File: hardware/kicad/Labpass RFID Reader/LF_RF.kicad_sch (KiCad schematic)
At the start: 24 parts

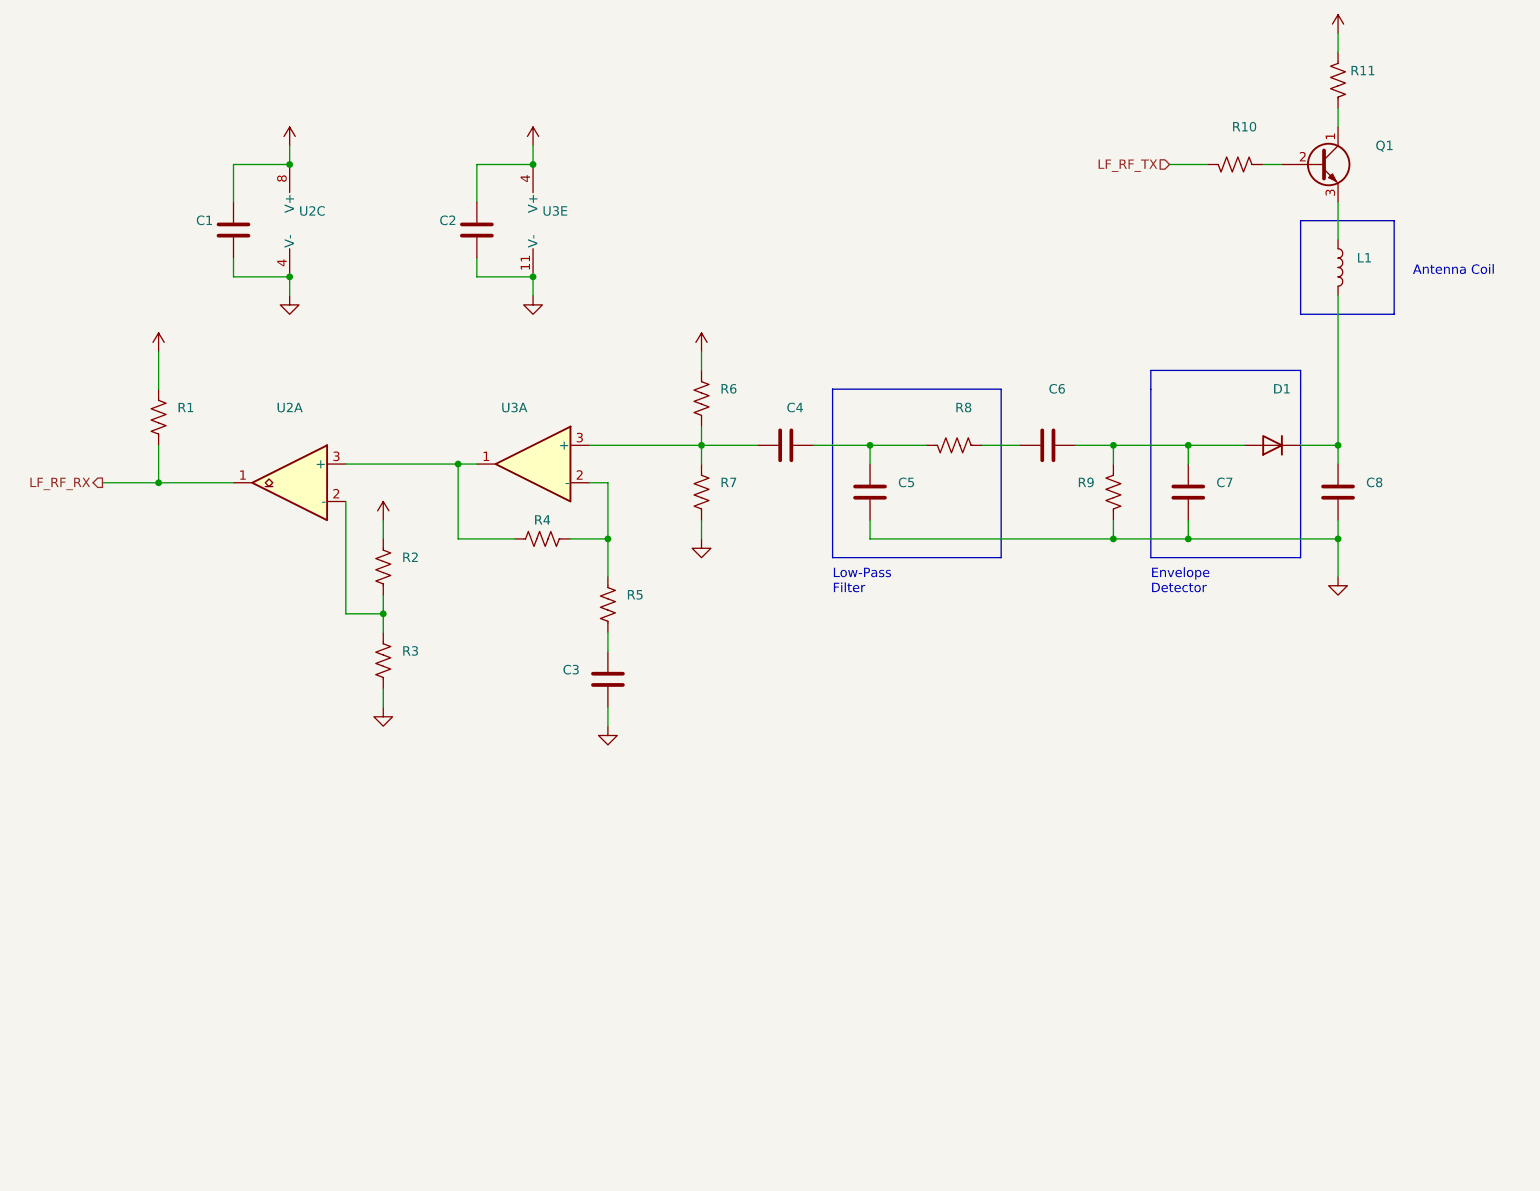
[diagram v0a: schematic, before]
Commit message: Re-do board design using kicad 6.04 stable
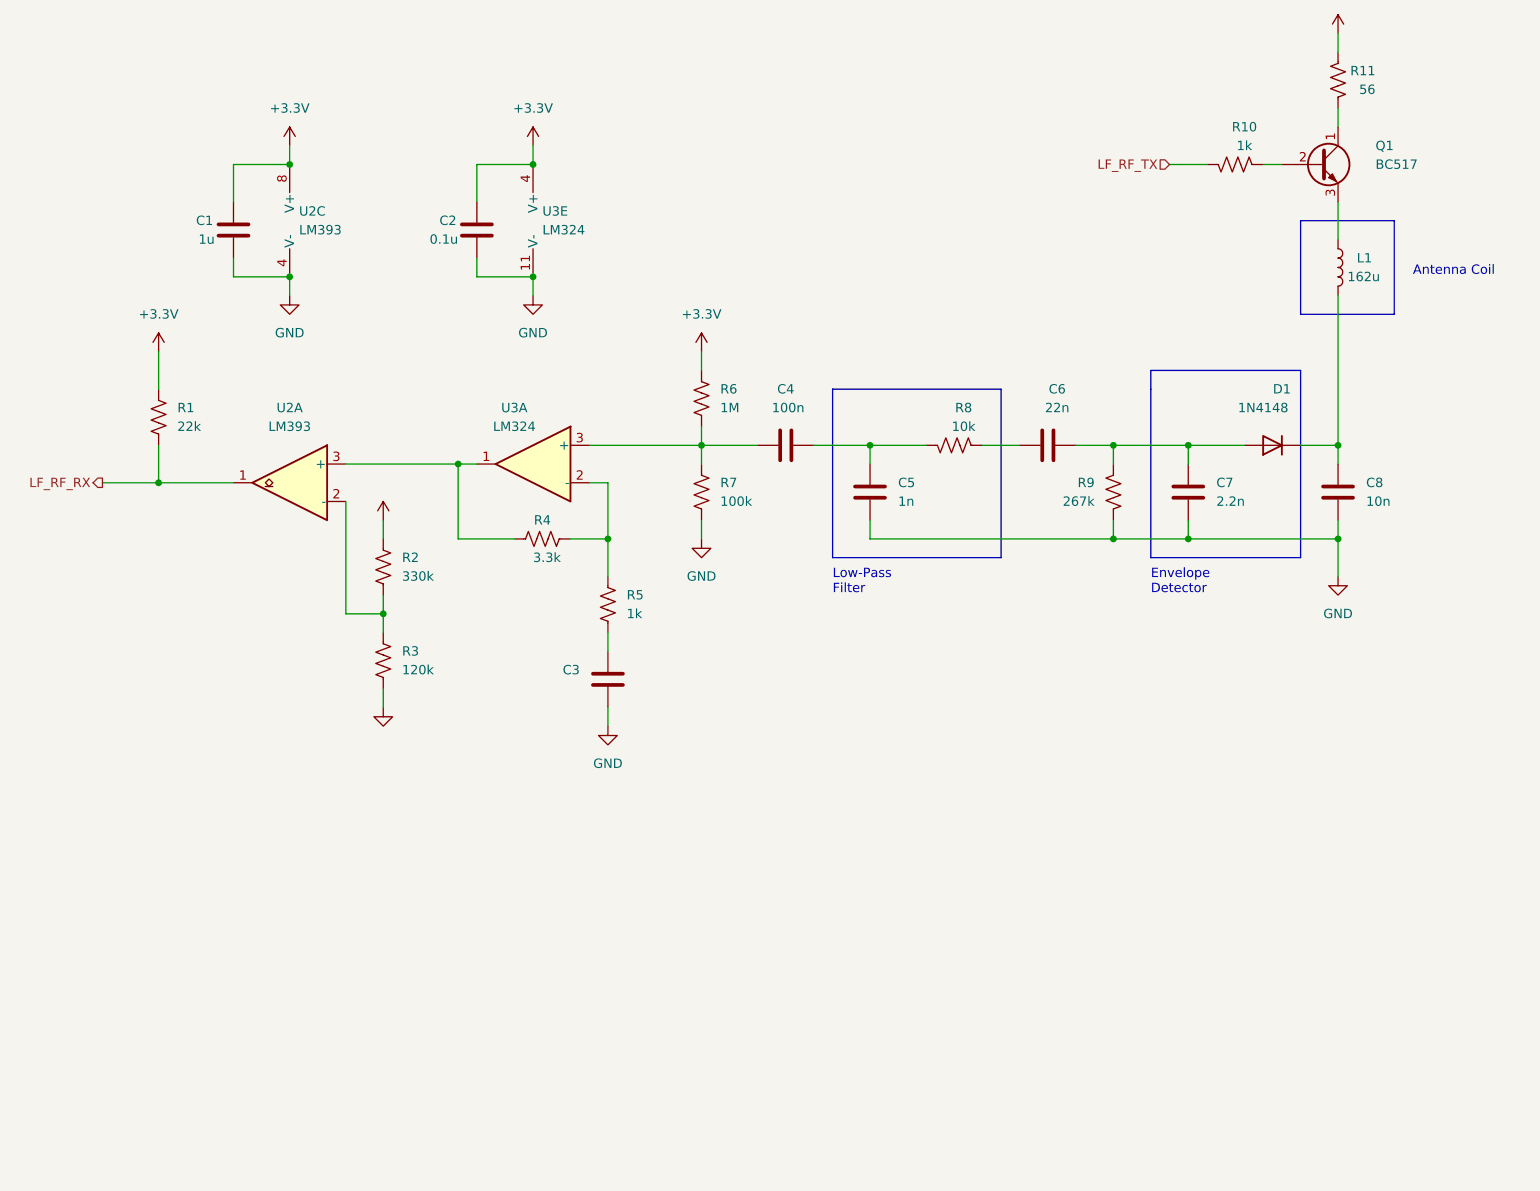
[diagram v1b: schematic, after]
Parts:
- C1: value (none) -> 1u; footprint (none) -> Capacitor_SMD:C_0603_1608Metric
- C2: value (none) -> 0.1u; footprint (none) -> Capacitor_SMD:C_0603_1608Metric
- C3: value (none) -> ~; footprint (none) -> Capacitor_SMD:C_0603_1608Metric
- C4: value (none) -> 100n; footprint (none) -> Capacitor_SMD:C_0603_1608Metric
- C5: value (none) -> 1n; footprint (none) -> Capacitor_SMD:C_0603_1608Metric
- C6: value (none) -> 22n; footprint (none) -> Capacitor_SMD:C_0603_1608Metric
- C7: value (none) -> 2.2n; footprint (none) -> Capacitor_SMD:C_0603_1608Metric
- C8: value (none) -> 10n; footprint (none) -> Capacitor_SMD:C_0603_1608Metric
- D1: value (none) -> 1N4148; footprint (none) -> Diode_SMD:D_SOD-323F
- L1: value (none) -> 162u; footprint (none) -> Connector_PinHeader_1.00mm:PinHeader_1x02_P1.00mm_Vertical_SMD_Pin1Left
- Q1: value (none) -> BC517; footprint (none) -> Package_TO_SOT_THT:TO-92
- R1: value (none) -> 22k; footprint (none) -> Resistor_SMD:R_0603_1608Metric
- R10, R5: value (none) -> 1k; footprint (none) -> Resistor_SMD:R_0603_1608Metric
- R11: value (none) -> 56; footprint (none) -> Resistor_SMD:R_0603_1608Metric
- R2: value (none) -> 330k; footprint (none) -> Resistor_SMD:R_0603_1608Metric
- R3: value (none) -> 120k; footprint (none) -> Resistor_SMD:R_0603_1608Metric
- R4: value (none) -> 3.3k; footprint (none) -> Resistor_SMD:R_0603_1608Metric
- R6: value (none) -> 1M; footprint (none) -> Resistor_SMD:R_0603_1608Metric
- R7: value (none) -> 100k; footprint (none) -> Resistor_SMD:R_0603_1608Metric
- R8: value (none) -> 10k; footprint (none) -> Resistor_SMD:R_0603_1608Metric
- R9: value (none) -> 267k; footprint (none) -> Resistor_SMD:R_0603_1608Metric
- U2: value (none) -> LM393; footprint (none) -> Package_SO:SOIC-8_3.9x4.9mm_P1.27mm
- U3: value (none) -> LM324; footprint (none) -> Package_SO:SO-14_3.9x8.65mm_P1.27mm

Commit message: kicad backups
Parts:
- removed L1: 162u, Connector_PinHeader_1.00mm:PinHeader_1x02_P1.00mm_Vertical_SMD_Pin1Left, symbol Device:L
- added J3: (no value), symbol Connector_Generic:Conn_01x02
- C1, C2: Temp Coef (none) -> X5R
- C3: value ~ -> 100n; Temp Coef (none) -> NP0
- C4, C5, C6, C7: Temp Coef (none) -> NP0
- C8: value 10n -> (none); footprint Capacitor_SMD:C_0603_1608Metric -> (none); Temp Coef (none) -> NP0
- R3: value 120k -> 110k
- R9: value 267k -> 222k
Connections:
- net at C8.1, D1.1 (K): now also J3.2 (Pin_2)
- net at Q1.3 (E): now also J3.1 (Pin_1)
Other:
- note added: "Hand-Wound rectangular coil approx 61mm X 61mm 26 AWG (.404mm dia) N = 25 L should be as close as possible to 162.1 uH"
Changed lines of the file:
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@@
     (stroke (width 0) (type default) (color 0 0 0 0))
   )
-  (polyline (pts (xy 226.06 66.04) (xy 238.76 66.04))
+  (polyline (pts (xy 227.33 66.04) (xy 240.03 66.04))
     (stroke (width 0) (type default) (color 0 0 0 0))
   )
@@
     (stroke (width 0) (type default) (color 0 0 0 0))
   )
-  (wire (pts (xy 231.14 76.2) (xy 231.14 96.52))
+  (wire (pts (xy 231.14 73.66) (xy 231.14 96.52))
     (stroke (width 0) (type default) (color 0 0 0 0))
   )
@@
     (stroke (width 0) (type default) (color 0 0 0 0))
   )
+  (polyline (pts (xy 240.03 66.04) (xy 246.38 66.04))
+    (stroke (width 0) (type default) (color 0 0 0 0))
+  )
   (wire (pts (xy 88.9 55.88) (xy 88.9 58.42))
     (stroke (width 0) (type default) (color 0 0 0 0))
@@
     (stroke (width 0) (type default) (color 0 0 0 0))
   )
-  (polyline (pts (xy 238.76 78.74) (xy 226.06 78.74))
+  (polyline (pts (xy 246.38 78.74) (xy 227.33 78.74))
     (stroke (width 0) (type default) (color 0 0 0 0))
   )
@@
     (stroke (width 0) (type default) (color 0 0 0 0))
   )
-  (wire (pts (xy 231.14 63.5) (xy 231.14 68.58))
+  (wire (pts (xy 231.14 63.5) (xy 231.14 71.12))
     (stroke (width 0) (type default) (color 0 0 0 0))
   )
@@
     (stroke (width 0) (type default) (color 0 0 0 0))
   )
-  (polyline (pts (xy 238.76 66.04) (xy 238.76 78.74))
+  (polyline (pts (xy 246.38 66.04) (xy 246.38 78.74))
     (stroke (width 0) (type default) (color 0 0 0 0))
   )
@@
     (stroke (width 0) (type default) (color 0 0 0 0))
   )
-  (polyline (pts (xy 226.06 66.04) (xy 226.06 78.74))
+  (polyline (pts (xy 227.33 66.04) (xy 227.33 78.74))
     (stroke (width 0) (type default) (color 0 0 0 0))
   )
@@
     (stroke (width 0) (type default) (color 0 0 0 0))
   )
-  (text "Antenna Coil" (at 241.3 73.66 0)
+  (text "Hand-Wound rectangular coil\napprox 61mm X 61mm \n26 AWG (.404mm dia)\nN = 25\nL should be as close as possible to \n162.1 uH"
+    (at 224.79 78.74 0)
+    (effects (font (size 1.27 1.27)) (justify right bottom))
+  )
+  (text "Antenna Coil" (at 236.22 82.55 0)
     (effects (font (size 1.27 1.27)) (justify left bottom))
   )
@@
       (effects (font (size 1.27 1.27)) (justify left))
     )
-    (property "Value" "120k" (id 1) (at 104.14 126.9999 0)
+    (property "Value" "110k" (id 1) (at 104.14 126.9999 0)
       (effects (font (size 1.27 1.27)) (justify left))
     )
@@
       (effects (font (size 1.27 1.27)) (justify right))
     )
-    (property "Value" "10n" (id 1) (at 234.95 104.1399 0)
-      (effects (font (size 1.27 1.27)) (justify right))
-    )
-    (property "Footprint" "Capacitor_SMD:C_0603_1608Metric" (id 2) (at 230.1748 106.68 0)
+    (property "Value" "" (id 1) (at 234.95 104.1399 0)
+      (effects (font (size 1.27 1.27)) (justify right))
+    )
+    (property "Footprint" "" (id 2) (at 230.1748 106.68 0)
       (effects (font (size 1.27 1.27)) hide)
     )
     (property "Datasheet" "~" (id 3) (at 231.14 102.87 0)
+      (effects (font (size 1.27 1.27)) hide)
+    )
+    (property "Temp Coef" "NP0" (id 4) (at 231.14 102.87 0)
       (effects (font (size 1.27 1.27)) hide)
     )
@@
       (effects (font (size 1.27 1.27)) hide)
     )
+    (property "Temp Coef" "NP0" (id 4) (at 191.77 96.52 0)
+      (effects (font (size 1.27 1.27)) hide)
+    )
     (pin "1")
     (pin "2")
@@
     )
     (property "Datasheet" "~" (id 3) (at 156.21 96.52 0)
+      (effects (font (size 1.27 1.27)) hide)
+    )
+    (property "Temp Coef" "NP0" (id 4) (at 156.21 96.52 0)
       (effects (font (size 1.27 1.27)) hide)
     )
@@
       (effects (font (size 1.27 1.27)) (justify right))
     )
-    (property "Value" "~" (id 1) (at 128.27 129.5399 0)
+    (property "Value" "100n" (id 1) (at 128.27 129.5399 0)
       (effects (font (size 1.27 1.27)) (justify right))
     )
@@
       (effects (font (size 1.27 1.27)) hide)
     )
+    (property "Temp Coef" "NP0" (id 4) (at 132.08 128.27 0)
+      (effects (font (size 1.27 1.27)) hide)
+    )
     (pin "1")
     (pin "2")
@@
     )
     (property "Datasheet" "~" (id 3) (at 167.64 102.87 0)
+      (effects (font (size 1.27 1.27)) hide)
+    )
+    (property "Temp Coef" "NP0" (id 4) (at 167.64 102.87 0)
       (effects (font (size 1.27 1.27)) hide)
     )
@@
       (effects (font (size 1.27 1.27)) (justify right))
     )
-    (property "Value" "267k" (id 1) (at 198.12 104.1399 0)
+    (property "Value" "222k" (id 1) (at 198.12 104.1399 0)
       (effects (font (size 1.27 1.27)) (justify right))
     )
@@
     )
     (property "Datasheet" "~" (id 3) (at 200.66 102.87 0)
-      (effects (font (size 1.27 1.27)) hide)
-    )
-    (pin "1")
-    (pin "2")
-  )
-  (symbol (lib_id "Device:L") (at 231.14 72.39 0) (unit 1)
-    (in_bom yes) (on_board yes)
-    (property "Reference" "L1" (id 0) (at 233.68 71.12 0)
-      (effects (font (size 1.27 1.27)) (justify left))
-    )
-    (property "Value" "162u" (id 1) (at 232.41 73.6599 0)
-      (effects (font (size 1.27 1.27)) (justify left))
-    )
-    (property "Footprint" "Connector_PinHeader_1.00mm:PinHeader_1x02_P1.00mm_Vertical_SMD_Pin1Left" (id 2) (at 231.14 72.39 0)
-      (effects (font (size 1.27 1.27)) hide)
-    )
-    (property "Datasheet" "~" (id 3) (at 231.14 72.39 0)
       (effects (font (size 1.27 1.27)) hide)
     )
@@
       (effects (font (size 1.27 1.27)) hide)
     )
+    (property "Temp Coef" "X5R" (id 4) (at 114.3 67.31 0)
+      (effects (font (size 1.27 1.27)) hide)
+    )
     (pin "1")
     (pin "2")
@@
     )
     (property "Datasheet" "~" (id 3) (at 101.6 113.03 0)
+      (effects (font (size 1.27 1.27)) hide)
+    )
+    (pin "1")
+    (pin "2")
+  )
+  (symbol (lib_id "Connector_Generic:Conn_01x02") (at 236.22 71.12 0) (unit 1)
+    (in_bom yes) (on_board yes) (fields_autoplaced)
+    (property "Reference" "J3" (id 0) (at 238.76 71.1199 0)
+      (effects (font (size 1.27 1.27)) (justify left))
+    )
+    (property "Value" "" (id 1) (at 238.76 73.6599 0)
+      (effects (font (size 1.27 1.27)) (justify left) hide)
+    )
+    (property "Footprint" "" (id 2) (at 236.22 71.12 0)
+      (effects (font (size 1.27 1.27)) hide)
+    )
+    (property "Datasheet" "~" (id 3) (at 236.22 71.12 0)
       (effects (font (size 1.27 1.27)) hide)
     )
@@
       (effects (font (size 1.27 1.27)) hide)
     )
+    (property "Temp Coef" "NP0" (id 4) (at 210.82 102.87 0)
+      (effects (font (size 1.27 1.27)) hide)
+    )
     (pin "1")
     (pin "2")
@@
       (effects (font (size 1.27 1.27)) hide)
     )
+    (property "Temp Coef" "X5R" (id 4) (at 81.28 67.31 0)
+      (effects (font (size 1.27 1.27)) hide)
+    )

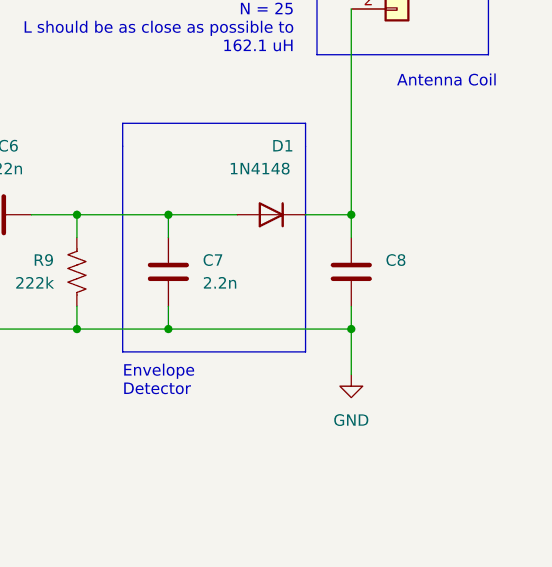
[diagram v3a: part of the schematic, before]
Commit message: add missing dc blocking cap to HF path
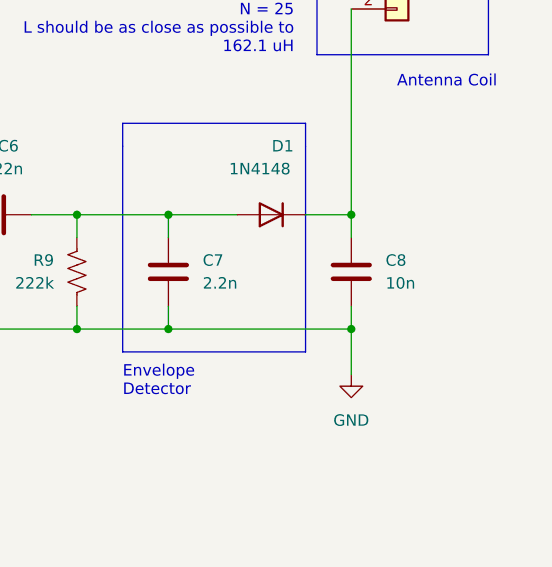
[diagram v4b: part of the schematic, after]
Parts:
- C8: value (none) -> 10n; footprint (none) -> Capacitor_SMD:C_0603_1608Metric
- J3: value (none) -> Conn_01x02; footprint (none) -> Connector_PinHeader_2.54mm:PinHeader_1x02_P2.54mm_Vertical_SMD_Pin1Left
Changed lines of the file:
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@@
       (effects (font (size 1.27 1.27)) (justify right))
     )
-    (property "Value" "" (id 1) (at 234.95 104.1399 0)
-      (effects (font (size 1.27 1.27)) (justify right))
-    )
-    (property "Footprint" "" (id 2) (at 230.1748 106.68 0)
+    (property "Value" "10n" (id 1) (at 234.95 104.1399 0)
+      (effects (font (size 1.27 1.27)) (justify right))
+    )
+    (property "Footprint" "Capacitor_SMD:C_0603_1608Metric" (id 2) (at 230.1748 106.68 0)
       (effects (font (size 1.27 1.27)) hide)
     )
@@
       (effects (font (size 1.27 1.27)) (justify left))
     )
-    (property "Value" "" (id 1) (at 238.76 73.6599 0)
+    (property "Value" "Conn_01x02" (id 1) (at 238.76 73.6599 0)
       (effects (font (size 1.27 1.27)) (justify left) hide)
     )
-    (property "Footprint" "" (id 2) (at 236.22 71.12 0)
-      (effects (font (size 1.27 1.27)) hide)
-    )
+    (property "Footprint" "Connector_PinHeader_2.54mm:PinHeader_1x02_P2.54mm_Vertical_SMD_Pin1Left" (id 2) (at 236.22 71.12 0)
+      (effects (font (size 1.27 1.27)) hide)
+    )

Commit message: Several fixes
* EA and I2C were backwards
* Adding missing Crx into HF receive path
* Better header size and placement
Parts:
- J3: value Conn_01x02 -> (none); footprint Connector_PinHeader_2.54mm:PinHeader_1x02_P2.54mm_Vertical_SMD_Pin1Left -> (none)
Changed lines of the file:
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@@
       (effects (font (size 1.27 1.27)) (justify left))
     )
-    (property "Value" "Conn_01x02" (id 1) (at 238.76 73.6599 0)
+    (property "Value" "" (id 1) (at 238.76 73.6599 0)
       (effects (font (size 1.27 1.27)) (justify left) hide)
     )
-    (property "Footprint" "Connector_PinHeader_2.54mm:PinHeader_1x02_P2.54mm_Vertical_SMD_Pin1Left" (id 2) (at 236.22 71.12 0)
+    (property "Footprint" "" (id 2) (at 236.22 71.12 0)
       (effects (font (size 1.27 1.27)) hide)
     )

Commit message: Additional Changes
* remove transistor on LF path and power coil directly
  from ESP TX pin at 3.3V
* add some test points around the HF path
* add some cheap pots on LF for tuning the amplifier bias
  and comparator threshold
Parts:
- removed Q1: BC517, Package_TO_SOT_THT:TO-92, symbol Device:Q_NPN_CBE
- removed R10: 1k, Resistor_SMD:R_0603_1608Metric, symbol Device:R_US
- removed R11: 56, Resistor_SMD:R_0603_1608Metric, symbol Device:R_US
- added RV1, RV2: (no value), symbol Device:R_Potentiometer_US
- added unit 2 of U2
- added unit 3 of U3
- added unit 2 of U3
- added unit 4 of U3
- R2: value 330k -> (none); footprint Resistor_SMD:R_0603_1608Metric -> (none)
- R3: value 110k -> (none); footprint Resistor_SMD:R_0603_1608Metric -> (none)
- R7: value 100k -> (none); footprint Resistor_SMD:R_0603_1608Metric -> (none)
- U2: value LM393 -> (none); footprint Package_SO:SOIC-8_3.9x4.9mm_P1.27mm -> (none)
- U3: value LM324 -> (none); footprint Package_SO:SO-14_3.9x8.65mm_P1.27mm -> (none)
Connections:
- net GND: now also RV1.2, RV2.2; no longer R3.2, R7.2
- net LF_RF_TX: now also J3.1 (Pin_1)
- new net: R7.2, RV2.1
- new net: R3.2, RV1.1
- no-connect marks 0 -> 14
